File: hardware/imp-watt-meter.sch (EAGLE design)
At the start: 76 parts, among them Q2 535-10200-1-ND, U1 LED_DUAL, U2 PHOTOTRANSISTOR0603, U3 ADE7953ACPZLONGPADS, U4 PHOTOTRANSISTOR0603, U5 LED_DUAL

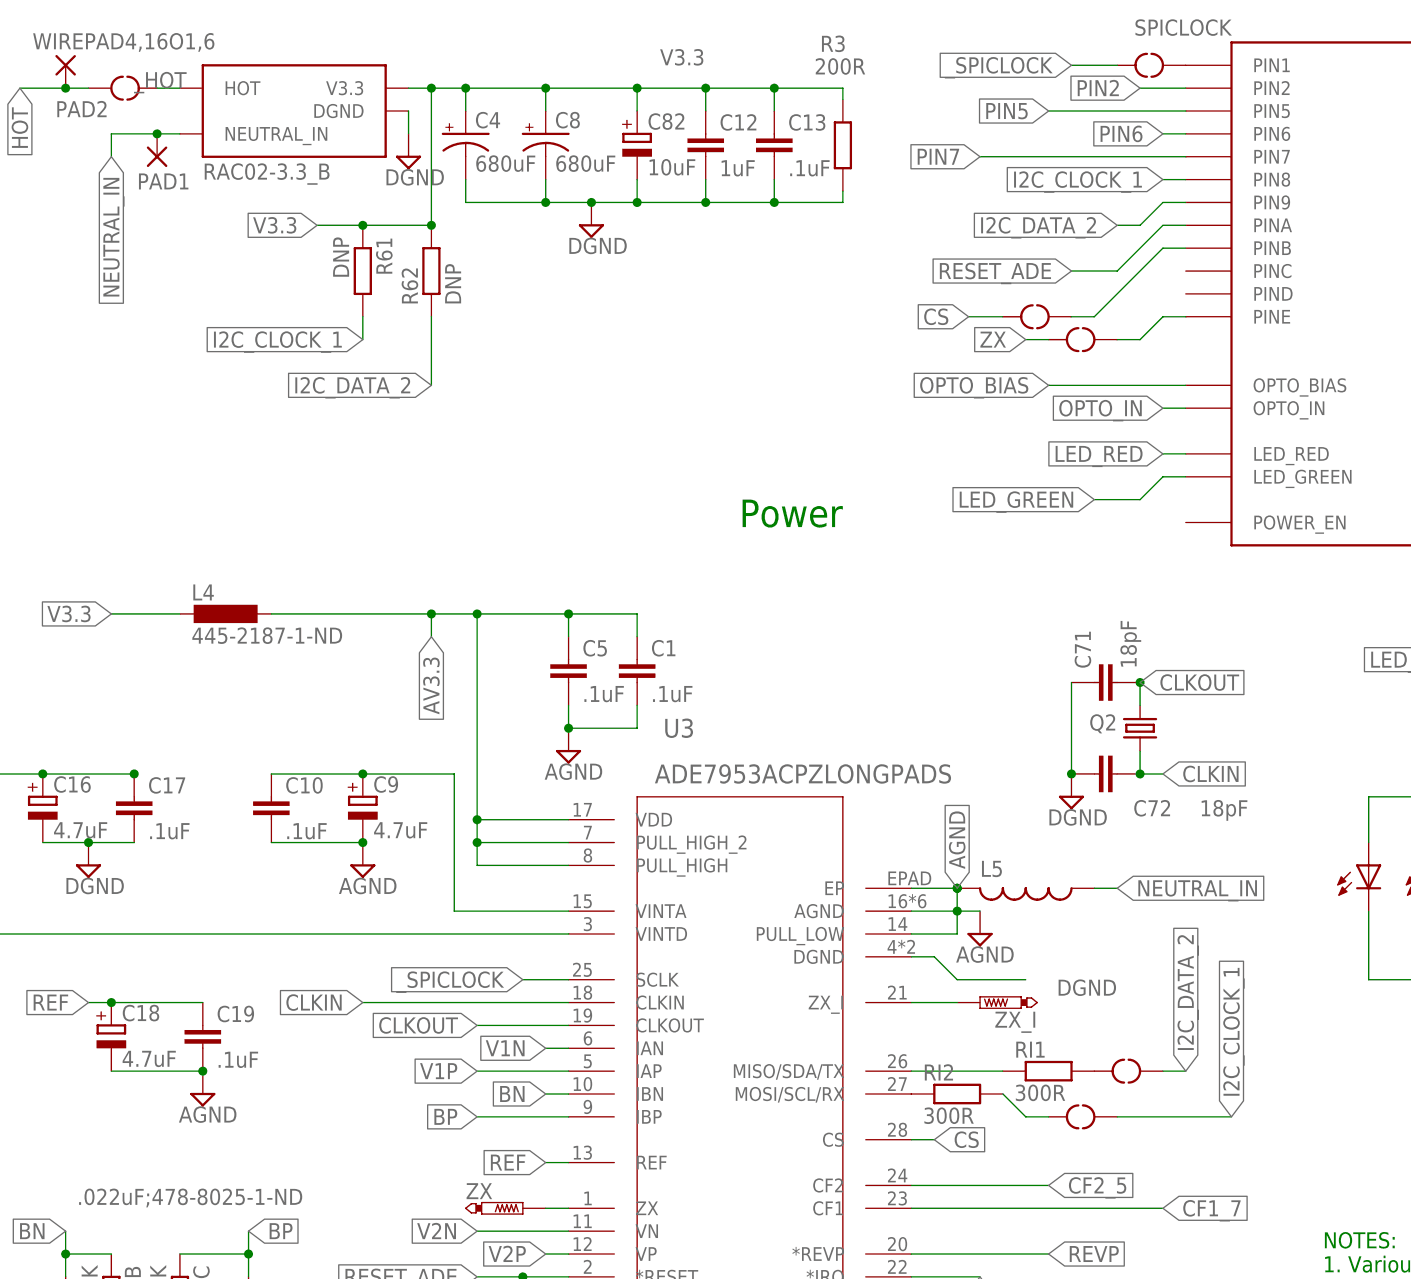
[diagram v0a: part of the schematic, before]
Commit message: reflect use of SPI, not i2c in name of nets
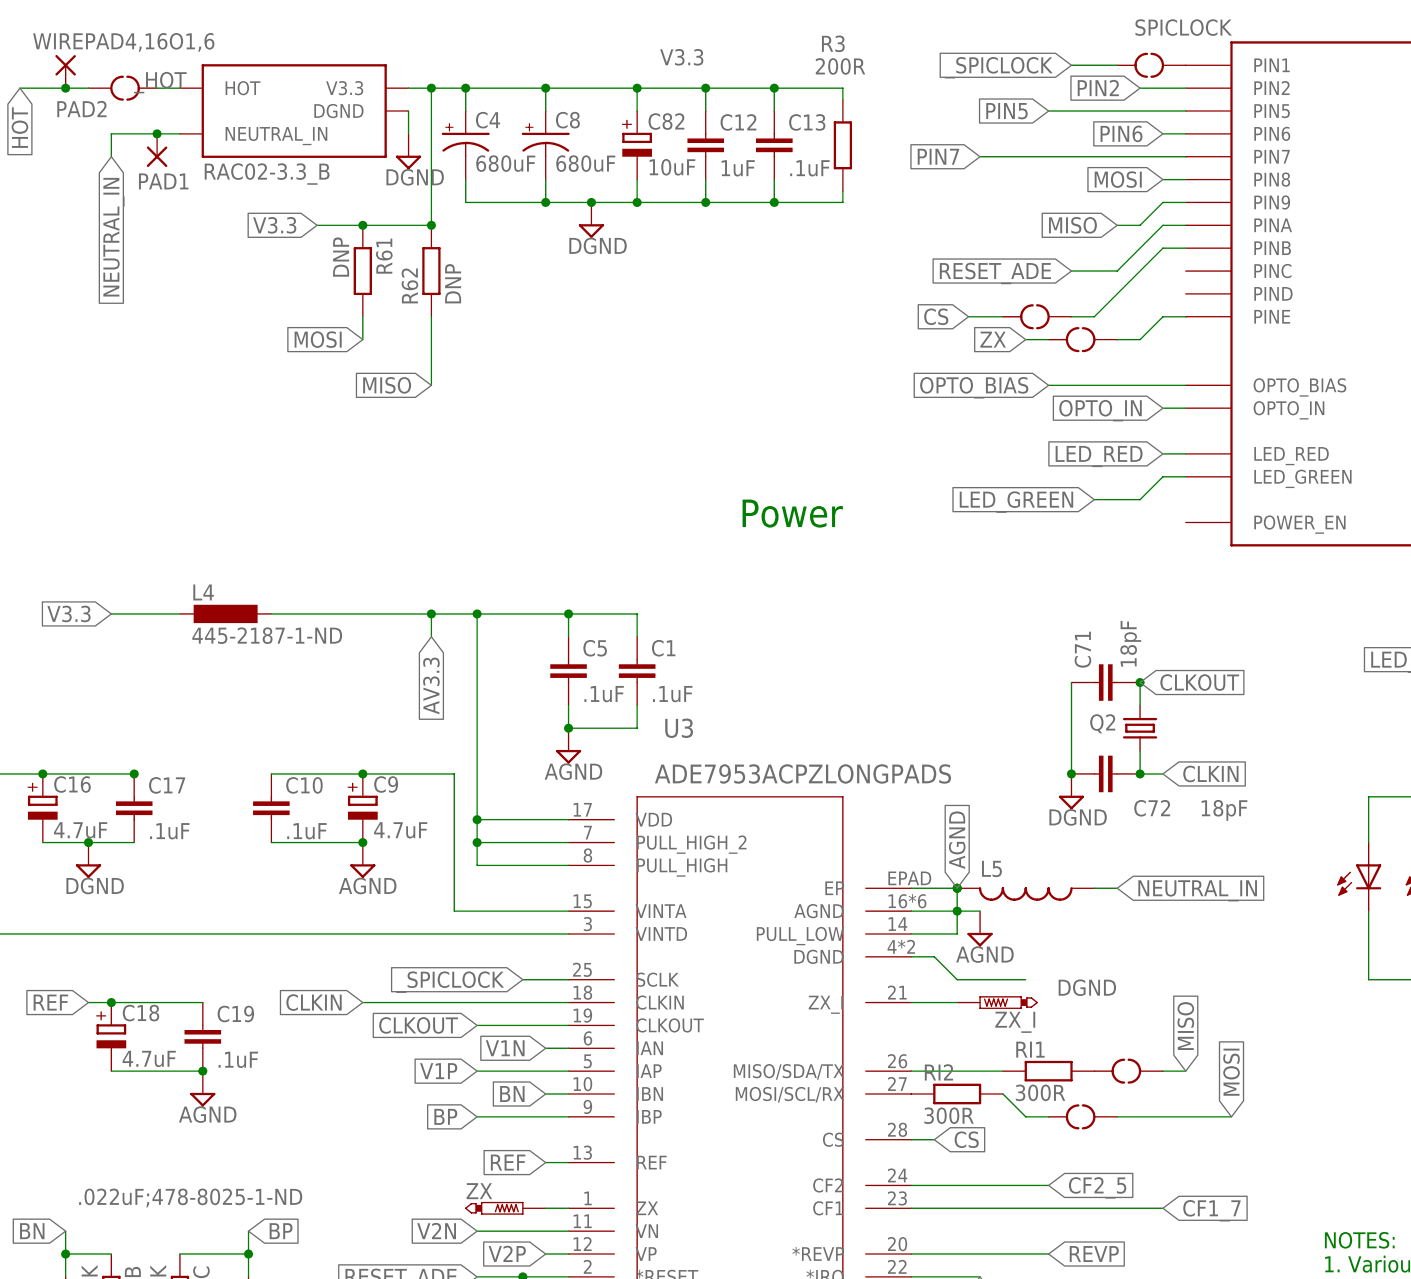
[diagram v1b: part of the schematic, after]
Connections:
- net I2C_CLOCK_1 renamed MOSI
- net I2C_DATA_2 renamed MISO
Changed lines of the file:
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@@
 <?xml version="1.0" encoding="utf-8"?>
 <!DOCTYPE eagle SYSTEM "eagle.dtd">
-<eagle version="7.4.0">
+<eagle version="7.1.0">
 <drawing>
 <settings>
@@
 </segment>
 </net>
-<net name="I2C_DATA_2" class="0">
+<net name="MISO" class="0">
 <segment>
 <label x="218.44" y="137.16" size="1.778" layer="95" rot="R180" xref="yes"/>
@@
 </segment>
 </net>
-<net name="I2C_CLOCK_1" class="0">
+<net name="MOSI" class="0">
 <segment>
 <label x="223.52" y="142.24" size="1.778" layer="95" rot="R180" xref="yes"/>

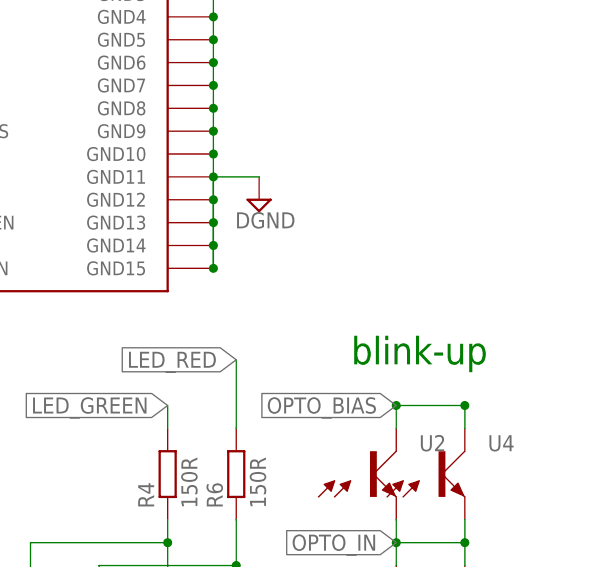
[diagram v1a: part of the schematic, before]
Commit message: clarified note on schematic
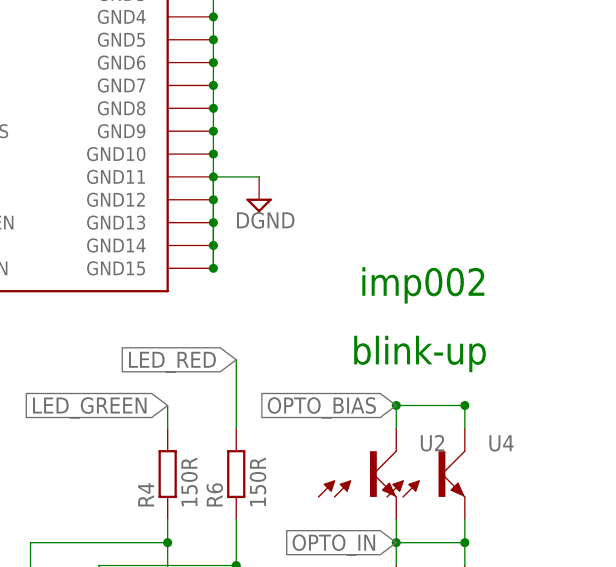
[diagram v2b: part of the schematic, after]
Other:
- note added: "imp002"
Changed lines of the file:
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@@
 <?xml version="1.0" encoding="utf-8"?>
 <!DOCTYPE eagle SYSTEM "eagle.dtd">
-<eagle version="7.1.0">
+<eagle version="7.4.0">
 <drawing>
 <settings>
@@
 operation.  Connect them as each sub-circuit
 is tested after reflow soldering.</text>
+<text x="297.18" y="104.14" size="3.048" layer="91" rot="R180">imp002</text>
 </plain>
 <instances>
